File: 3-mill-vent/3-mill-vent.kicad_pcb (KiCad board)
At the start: 2 copper layers, 90.2 x 54.6 mm, 59 parts, among them J1 ICSP, J2 Fan, J3 Buzzer, J4 POWER, Q1 MMBT3904, Q2 MMBT3904, Q3 PZT3904, Q4 PZT3904, Q5 TSM480P06CP, Q6 MMBT3904, SW1 Power_off, SW2 Power_On, SW3 Fan_Down, SW4 Fan_Up, U1 ATmega328P-AU, U2 TSR_1-24120, U3 LM1117-5.0, U4 LM321, Y1 ABLS7M-16.000MHZ-B-2-T

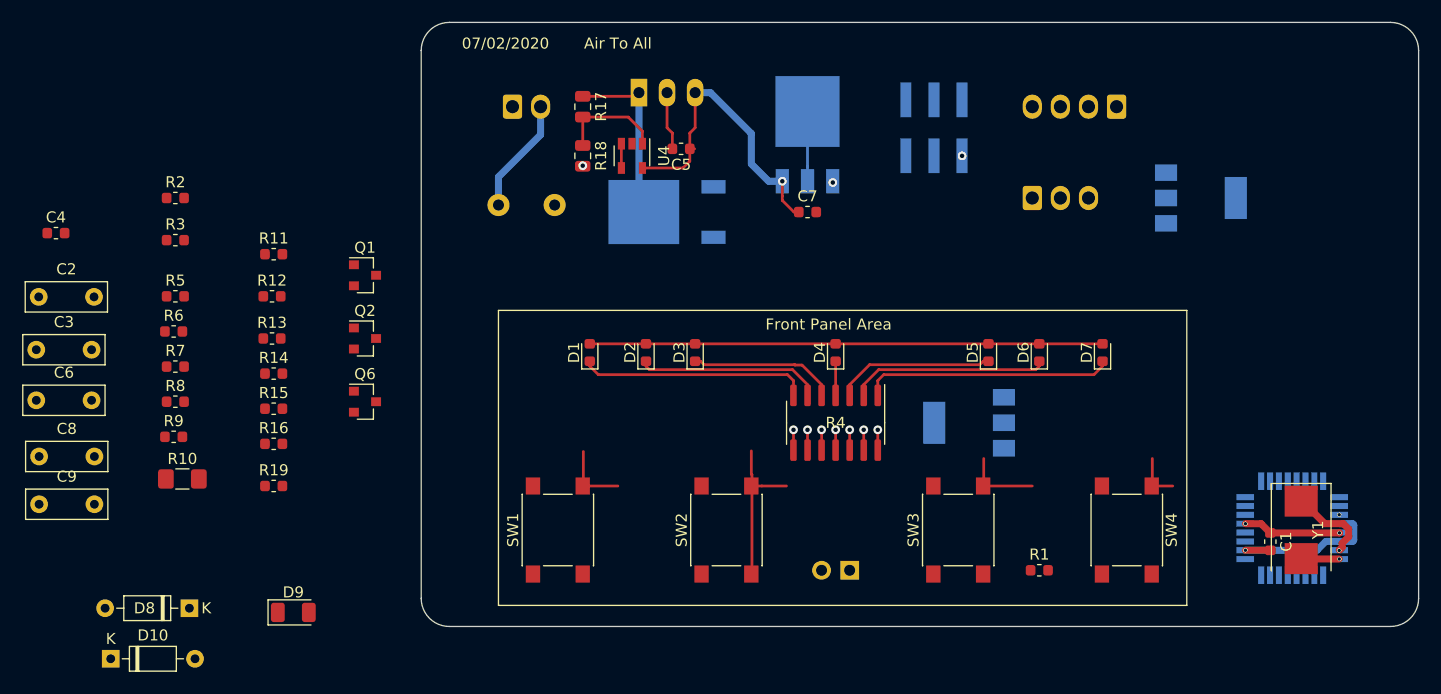
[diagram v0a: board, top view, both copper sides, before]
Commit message: Just a check point
More work done on all in one board.
Now has step file of board with traces
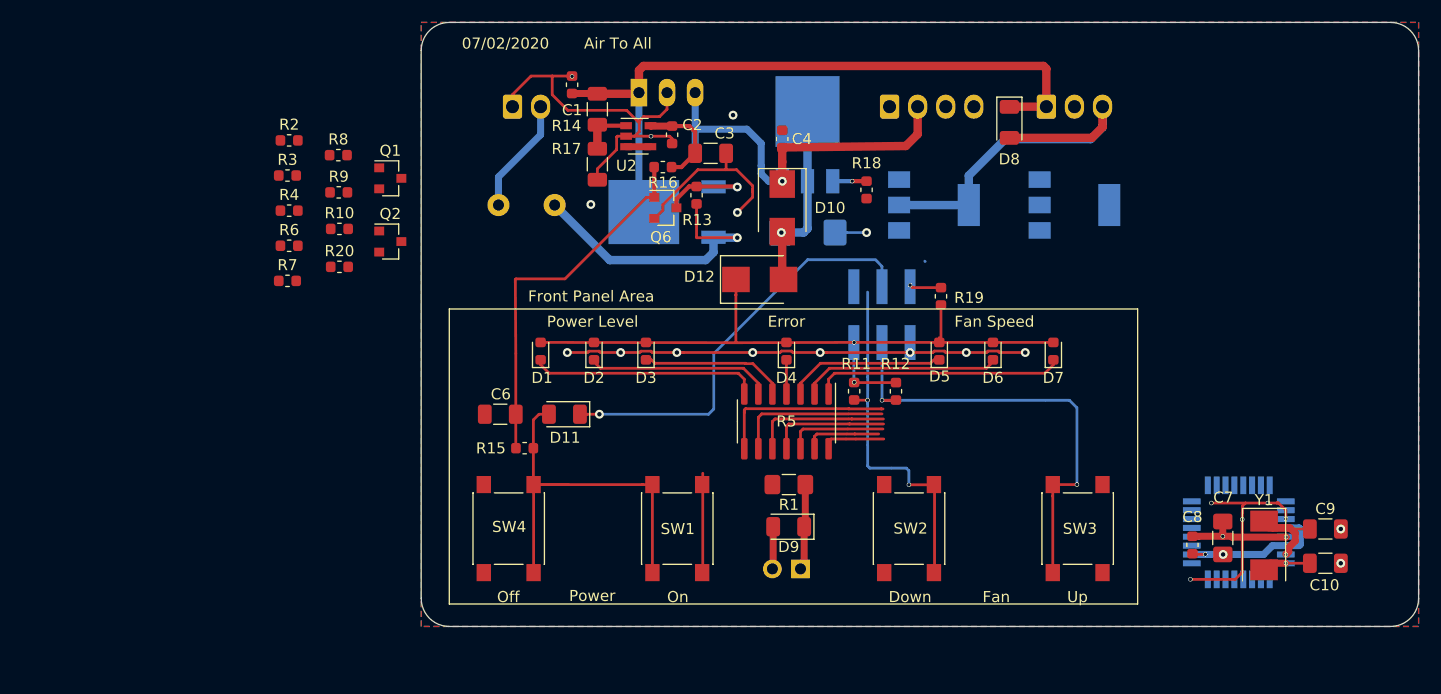
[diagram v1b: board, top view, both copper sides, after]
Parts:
- removed the U1 at (299.1, 109.2)
- added C4: C0603C104M4RACTU, Capacitor_SMD:C_0603_1608Metric, F.Cu at (253.0, 74.0)
- added D10: FM4004-W, Diode_SMD:D_SMB, F.Cu at (253.0, 80.3)
- added D12: FM4004-W, Diode_SMD:D_SMB, F.Cu at (251.0, 86.7)
- added R18: 47, Resistor_SMD:R_0603_1608Metric, F.Cu at (260.6, 78.6)
- added U4: ATmega328P-AU, Package_QFP:TQFP-32_7x7mm_P0.8mm, B.Cu at (294.3, 109.6)
- C10: renamed from C3; value 1uF -> 1206Y0160180FFT; footprint Capacitor_THT:C_Rect_L7.2mm_W2.5mm_P5.00mm_FKS2_FKP2_MKS2_MKP2 -> Capacitor_SMD:C_1206_3216Metric
- C3: renamed from C6; value 1uF -> LMK316AB7106MLHT; footprint Capacitor_THT:C_Rect_L7.2mm_W2.5mm_P5.00mm_FKS2_FKP2_MKS2_MKP2 -> Capacitor_SMD:C_1206_3216Metric
- C5: renamed from C8; value 10uF -> T491C107M006AT; footprint Capacitor_THT:C_Rect_L7.2mm_W2.5mm_P5.00mm_FKS2_FKP2_MKS2_MKP2 -> Capacitor_Tantalum_SMD:CP_EIA-6032-15_Kemet-U; moved to B.Cu
- C6: renamed from C9; footprint Capacitor_THT:C_Rect_L7.2mm_W2.5mm_P5.00mm_FKS2_FKP2_MKS2_MKP2 -> Capacitor_SMD:C_1206_3216Metric
- C7: value C0603C104M4RACTU -> LMK316AB7106MLHT; footprint Capacitor_SMD:C_0603_1608Metric -> Capacitor_SMD:C_1206_3216Metric_Pad1.42x1.75mm_HandSolder
- C9: renamed from C2; value 1uF -> 1206Y0160180FFT; footprint Capacitor_THT:C_Rect_L7.2mm_W2.5mm_P5.00mm_FKS2_FKP2_MKS2_MKP2 -> Capacitor_SMD:C_1206_3216Metric
- D11: renamed from D10; footprint Diode_THT:D_DO-35_SOD27_P7.62mm_Horizontal -> Diode_SMD:D_1206_3216Metric
- D7: value Fault -> Error
- D8: footprint Diode_THT:D_DO-35_SOD27_P7.62mm_Horizontal -> Diode_SMD:D_1206_3216Metric
- R14: renamed from R17; value RN73H2ATTD3302D25 -> RN73H2BTTD4702B10; footprint Resistor_SMD:R_0805_2012Metric -> Resistor_SMD:R_1206_3216Metric
- R17: renamed from R18; value RN73H2ATTD8201F25 -> RN73H2BTTD7061B10; footprint Resistor_SMD:R_0805_2012Metric -> Resistor_SMD:R_1206_3216Metric
- Y1: value ABLS7M-16.000MHZ-B-2-T -> 16.000MHZ; footprint Crystal:Crystal_SMD_7050-2Pin_7.0x5.0mm -> Crystal:Crystal_SMD_0603-2Pin_6.0x3.5mm
- moved C9 118.2 mm to (302.1, 109.3)
- moved C10 118.1 mm to (302.1, 112.4)
- moved D8 86.2 mm to (273.5, 72.5), turned to 270 degrees
- moved C5 72.4 mm to (255.3, 82.5)
- moved R19 69.4 mm to (267.3, 88.3), turned to 270 degrees
- moved R12 67.4 mm to (263.3, 96.9), turned to 90 degrees
- moved C3 64.9 mm to (246.5, 75.3)
- moved R1 54.8 mm to (253.6, 105.3), turned to 180 degrees
- moved C1 48.5 mm to (234.0, 69.1), turned to 90 degrees
- moved C7 47.7 mm to (292.8, 110.1), turned to 270 degrees
- moved D11 46.6 mm to (233.3, 98.9), turned to 180 degrees
- moved D9 45.4 mm to (253.6, 109.1), turned to 180 degrees
- moved C6 42.5 mm to (227.5, 98.9), turned to 180 degrees
- moved R13 41.5 mm to (245.2, 79.1), turned to 90 degrees
- moved R16 41.4 mm to (242.2, 76.6)
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- renumbered C4 to C1, C5 to C2, C1 to C8, R10 to R1, R13 to R10, R1 to R11, R2 to R12, R14 to R13, R16 to R15, R15 to R16, R3 to R19, R5 to R2, R19 to R20, R6 to R3, R7 to R4, R4 to R5, R8 to R6, R9 to R7, R11 to R8, R12 to R9, SW2 to SW1, SW3 to SW2, SW4 to SW3, SW1 to SW4, U2 to U1, U4 to U2
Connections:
- C5 pad 1: +5V -> Net-(C5-Pad1)
- C6 pad 1: Net-(C9-Pad1) (its old number) -> Net-(C6-Pad1)
- C7 pad 1: +12V -> GND
- C7 pad 2: GND -> +5V
- D11 pad 1: Net-(D10-Pad1) -> Monitor
- D11 pad 2: Monitor -> Net-(D11-Pad2)
- Q6 pad 1: Net-(C9-Pad1) (its old number) -> Net-(C6-Pad1)
- R15 pad 1: Net-(D10-Pad1) -> Net-(C6-Pad1)
- R15 pad 2: Net-(C9-Pad1) (its old number) -> Net-(D11-Pad2)
- R16 pad 1: Net-(C9-Pad1) (its old number) -> Net-(C6-Pad1)
- SW1 pad 1: Net-(C9-Pad1) (its old number) -> Net-(D11-Pad2)
- SW4 pad 2: Net-(C9-Pad1) (its old number) -> Net-(D11-Pad2)
- U3 pad 1: GND -> Net-(R18-Pad2)
- U3 pad 2: +5V -> Net-(C5-Pad1)
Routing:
- net GND: track 18.5 -> 124.8 mm, vias 6 -> 22
- net SW_Batt: track 16.2 -> 63.4 mm
- net Up: track 0.00 -> 41.5 mm, vias 0 -> 2
- net Monitor: track 0.00 -> 38.1 mm, vias 0 -> 1
- net Net-(D11-Pad2): track 0.00 -> 37.3 mm
- net Buzzer-: track 0.00 -> 35.4 mm
- net Net-(C6-Pad1): track 0.00 -> 33.6 mm
- net Raw_Batt: track 0.00 -> 27.0 mm, vias 0 -> 1
- net Down: track 6.87 -> 32.4 mm, vias 0 -> 2
- net Net-(C5-Pad1): track 0.00 -> 20.9 mm, vias 0 -> 1
- net +12V: track 27.8 -> 44.3 mm
- net LED1: track 1.84 -> 16.1 mm, vias 1 -> 0
- net LED2: track 1.84 -> 14.1 mm, vias 1 -> 0
- net LED3: track 1.84 -> 12.6 mm, vias 1 -> 0
- net +5V: track 67.8 -> 77.5 mm, vias 1 -> 4
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- added copper zone on B.Cu, net GND
- added copper zone on F.Cu, net GND
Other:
- board text added: "Alternative Micro Area"
- board text added: "Down"
- board text added: "Error"
- board text added: "Fan"
- board text added: "Fan Speed"
- board text added: "Off"
- board text added: "On"
- board text added: "Power"
- board text added: "Power Level"
- board text added: "Up"
